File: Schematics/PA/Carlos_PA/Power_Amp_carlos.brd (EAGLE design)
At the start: 83.5 x 71.1 mm, 105 parts, among them J1 4_PIN_AMPCONN, U1 LME49830, U2 LME49830, U3 LME49830

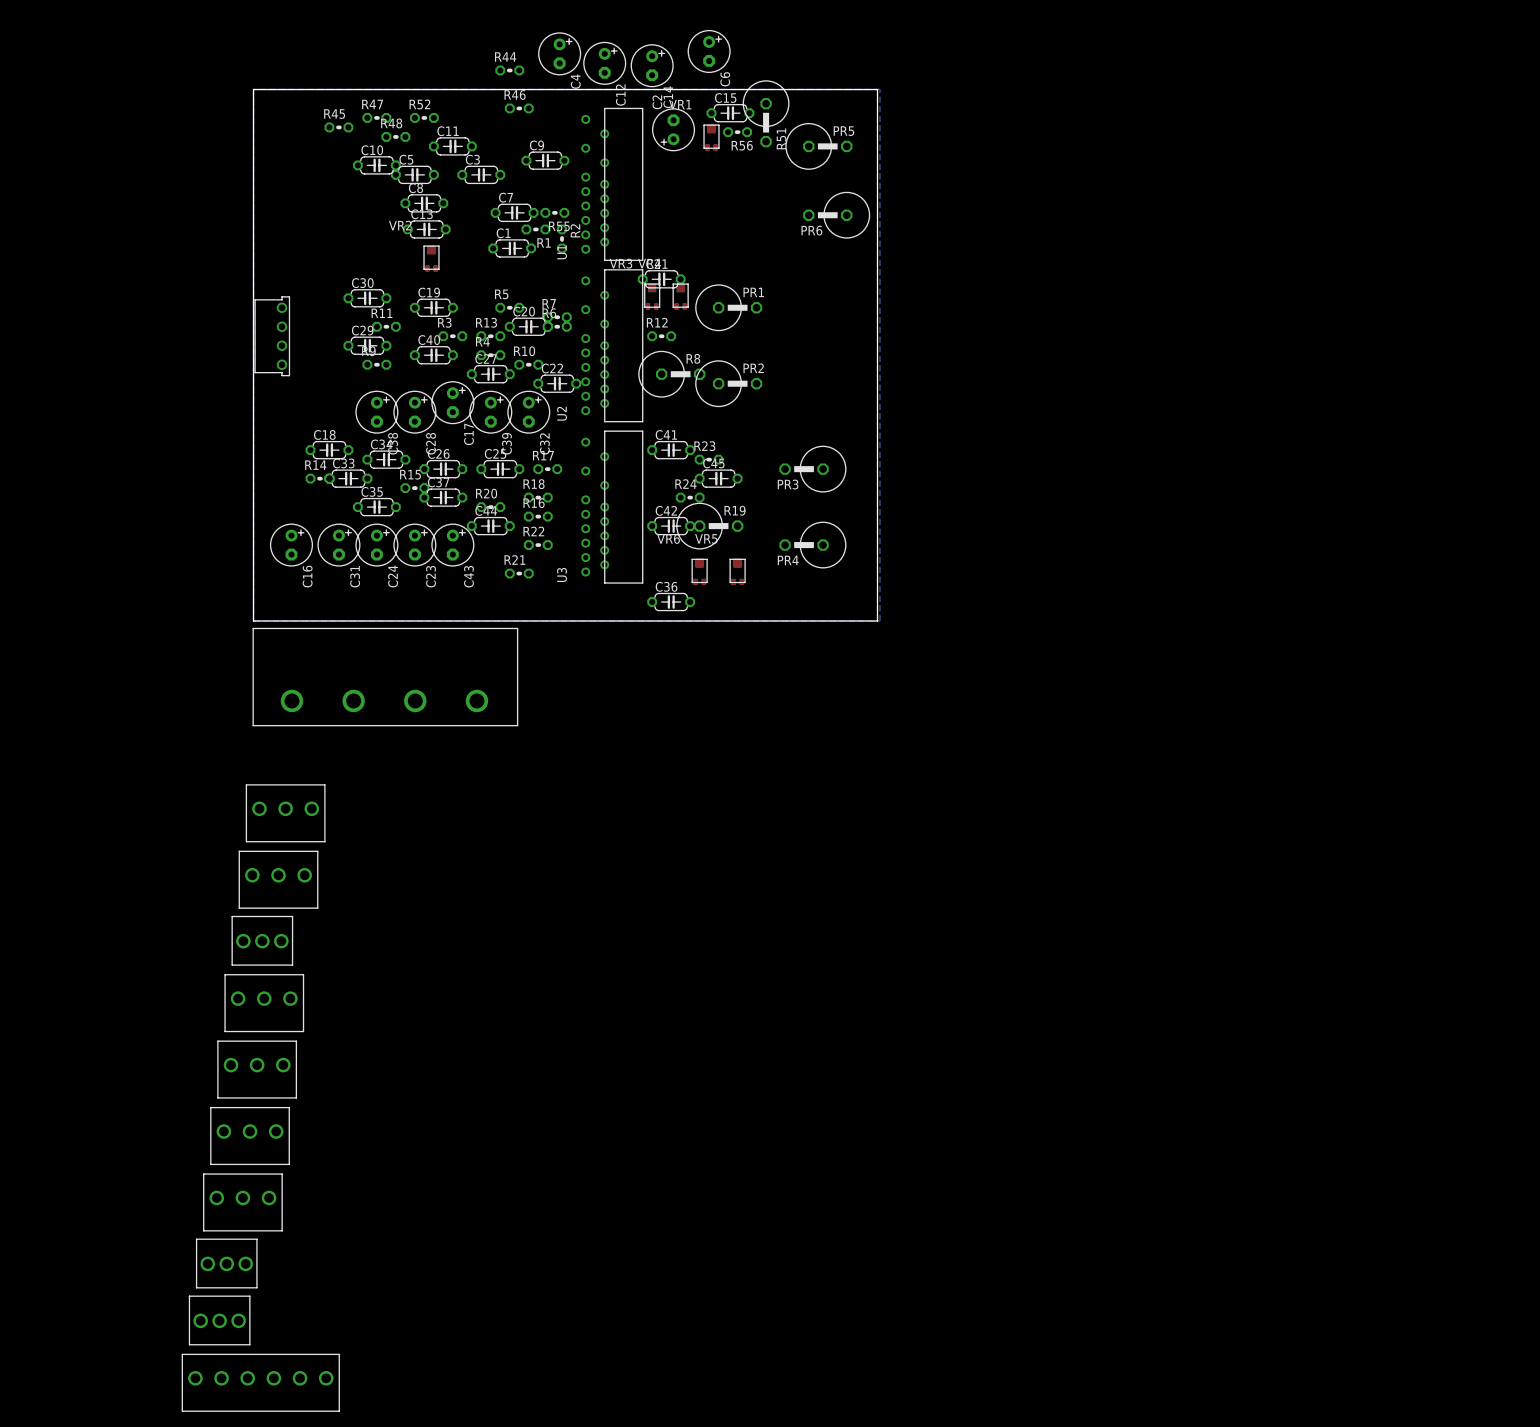
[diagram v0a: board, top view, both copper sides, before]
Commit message: fixed footprint of PA
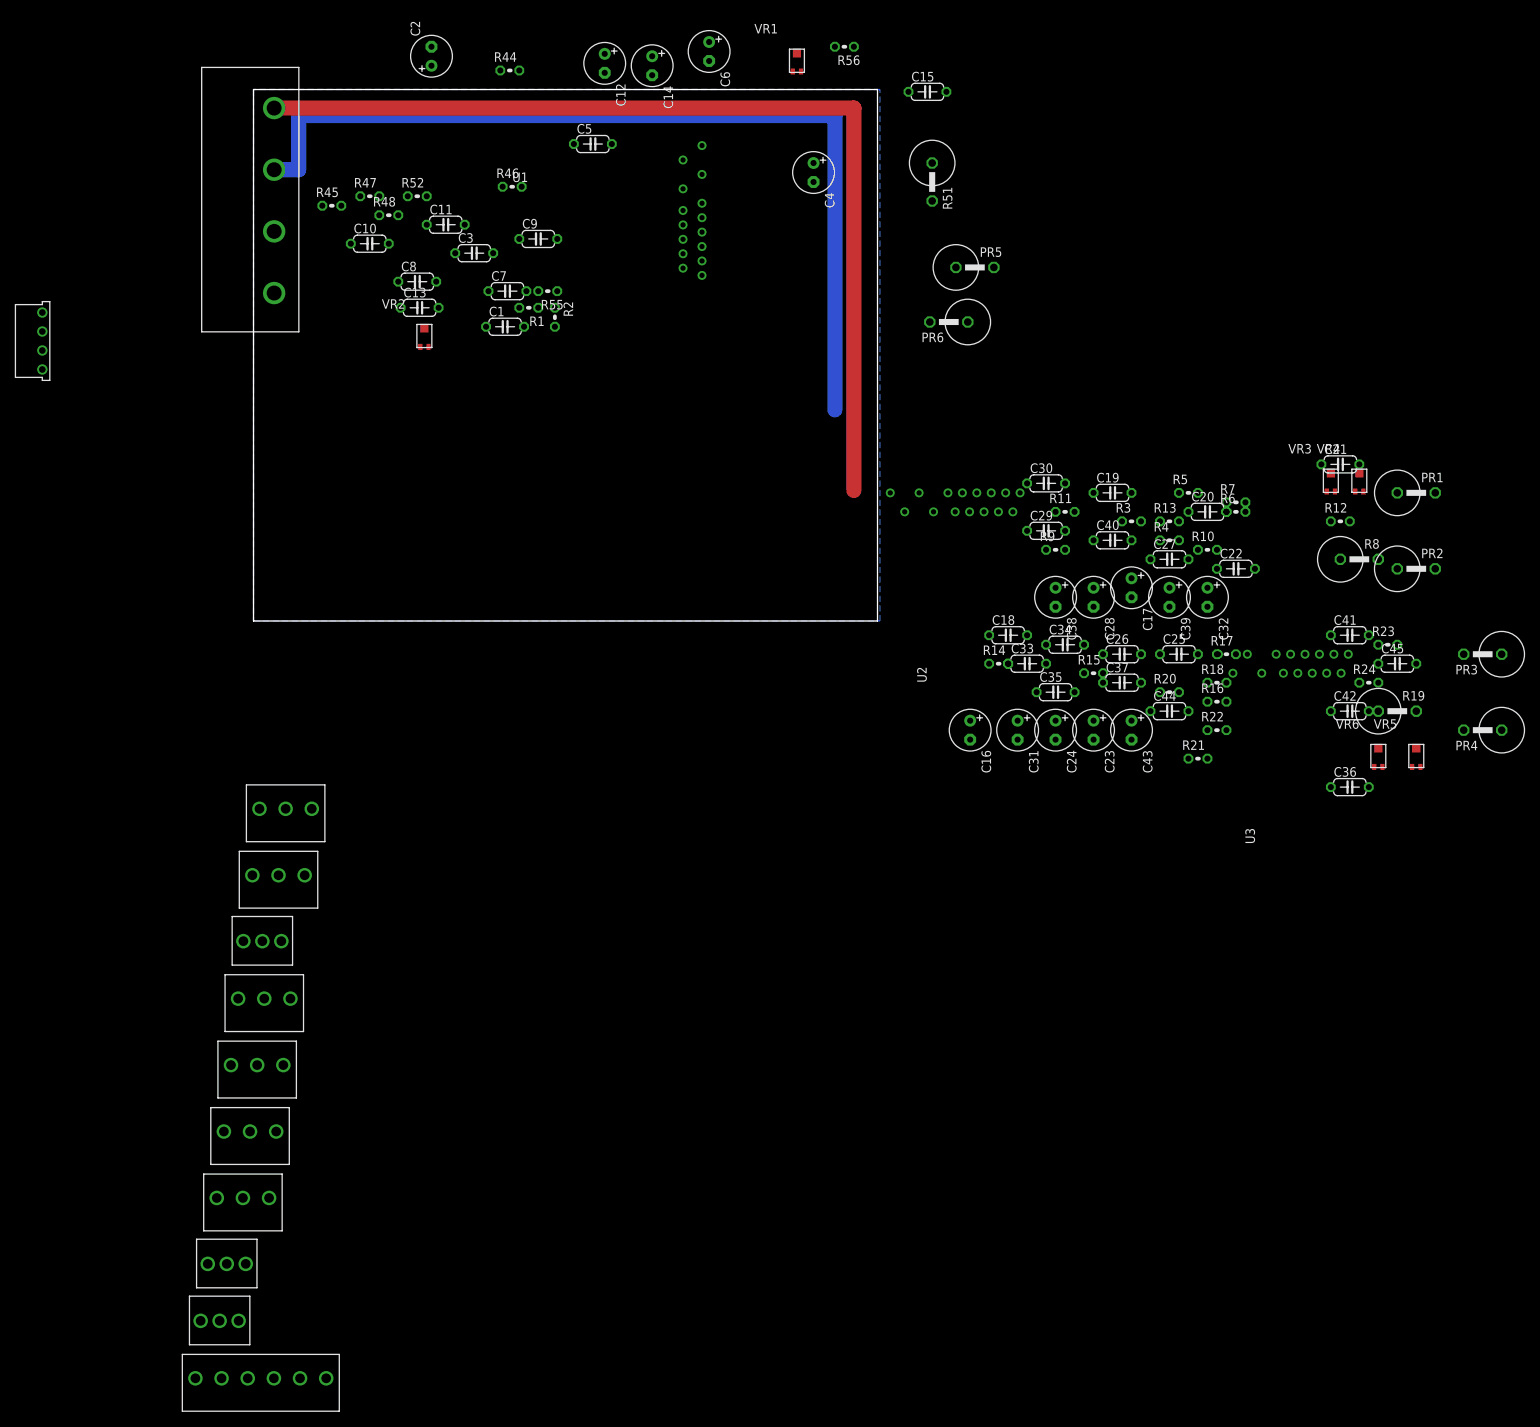
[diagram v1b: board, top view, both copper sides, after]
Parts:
- moved C16 94.1 mm to (95.9, -14.6)
- moved C18 94.1 mm to (101.0, -1.91)
- moved C19 94.1 mm to (114.9, 17.1)
- moved C20 94.1 mm to (127.6, 14.6)
- moved C25 94.1 mm to (123.8, -4.45)
- moved C26 94.1 mm to (116.2, -4.45)
- moved C27 94.1 mm to (122.6, 8.26)
- moved C29 94.1 mm to (106.0, 12.1)
- moved C30 94.1 mm to (106.0, 18.4)
- moved C31 94.1 mm to (102.2, -14.6)
- moved C32 94.1 mm to (127.6, 3.17)
- moved C36 94.1 mm to (146.7, -22.2)
- moved C37 94.1 mm to (116.2, -8.26)
- moved C39 94.1 mm to (122.6, 3.17)
- moved C40 94.1 mm to (114.9, 10.8)
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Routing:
- net V+: track 0.00 -> 128.7 mm
- net V-: track 0.00 -> 121.6 mm

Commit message: did dome work on my PA board
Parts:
- moved C47 119.6 mm to (70.2, 66.7), turned to 270 degrees
- moved C48 113.3 mm to (55.9, 59.1), turned to 270 degrees
- moved U3 97.9 mm to (42.2, 11.7), turned to 0 degrees
- moved U2 56.2 mm to (41.9, 33.4), turned to 0 degrees
- moved R48 48.4 mm to (66.0, 61.0), turned to 90 degrees
- moved R47 43.9 mm to (59.1, 62.5), turned to 90 degrees
- moved C11 41.3 mm to (65.1, 65.4), turned to 180 degrees
- moved C15 35.0 mm to (65.4, 46.0)
- moved C13 34.6 mm to (54.6, 54.0)
- moved C4 31.5 mm to (43.8, 65.1), turned to 0 degrees
- moved C9 30.4 mm to (12.4, 34.9)
- moved PR5 30.0 mm to (67.0, 52.4)
- moved R46 27.7 mm to (62.2, 59.7)
- moved C12 26.3 mm to (70.5, 62.9)
- moved PR6 26.2 mm to (71.4, 54.9), turned to 315 degrees
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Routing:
- net N$4: track 0.00 -> 33.1 mm
- net V+: track 128.7 -> 159.7 mm
- net V-: track 121.6 -> 148.5 mm, vias 0 -> 1
- net N$70: track 0.00 -> 22.4 mm
- net N$72: track 0.00 -> 13.0 mm
- net N$73: track 0.00 -> 11.5 mm
- net N$110: track 0.00 -> 9.09 mm
- net N$75: track 0.00 -> 8.19 mm
- net N$74: track 0.00 -> 5.35 mm

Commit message: more work on my Pa brd
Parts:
- moved C46 106.7 mm to (42.5, 50.5)
- moved J1 49.8 mm to (21.3, 32.4)
- moved C10 45.3 mm to (52.1, 59.7), turned to 180 degrees
- moved C6 44.9 mm to (27.9, 45.7), turned to 90 degrees
- moved R56 42.8 mm to (45.1, 50.8)
- moved R45 41.4 mm to (51.4, 56.5)
- moved VR1 39.5 mm to (41.0, 51.1)
- moved C9 37.8 mm to (41.3, 59.4), turned to 180 degrees
- moved VR2 31.8 mm to (47.3, 58.1)
- moved C8 23.4 mm to (42.5, 56.5)
- moved R44 21.9 mm to (53.0, 62.2)
- moved C7 21.6 mm to (47.9, 47.9), turned to 180 degrees
- moved R2 17.5 mm to (29.5, 50.8)
- moved U2 16.5 mm to (57.5, 28.0)
- moved U$5 16.2 mm to (19.7, 57.1)
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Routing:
- net N$75: track 8.19 -> 81.7 mm
- net N$85: track 0.00 -> 25.3 mm
- net N$69: track 0.00 -> 21.9 mm
- net MUTE: track 0.00 -> 18.4 mm
- net V+: track 159.7 -> 141.4 mm
- net N$67: track 0.00 -> 18.3 mm
- net N$65: track 0.00 -> 12.7 mm, vias 0 -> 1
- net N$66: track 0.00 -> 11.6 mm
- net N$68: track 0.00 -> 10.1 mm
- net N$16: track 0.00 -> 8.94 mm
- net N$31: track 0.00 -> 7.09 mm
- net N$40: track 0.00 -> 5.82 mm
- net N$36: track 0.00 -> 3.49 mm
- net V-: track 148.5 -> 151.9 mm, vias 1 -> 0

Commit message: finished my PA board
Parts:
- moved C55 179.6 mm to (81.3, 49.2), turned to 270 degrees
- moved C50 127.7 mm to (67.3, 41.6), turned to 270 degrees
- moved C53 122.5 mm to (41.9, 22.9)
- moved R12 108.0 mm to (37.8, 22.5)
- moved C49 106.4 mm to (52.7, 35.2), turned to 270 degrees
- moved VR3 105.4 mm to (39.4, 29.5)
- moved R10 103.8 mm to (25.1, 25.7)
- moved VR4 103.0 mm to (46.0, 33.3)
- moved C21 95.2 mm to (51.1, 34.3), turned to 180 degrees
- moved C22 94.1 mm to (41.3, 34.0)
- moved C19 93.2 mm to (26.4, 46.0), turned to 180 degrees
- moved PR1 93.0 mm to (63.2, 27.6)
- moved C28 91.6 mm to (25.7, 32.7), turned to 180 degrees
- moved PR2 91.1 mm to (67.6, 30.8), turned to 315 degrees
- moved C20 89.3 mm to (41.3, 37.1), turned to 180 degrees
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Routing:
- net N$12: track 0.00 -> 84.7 mm, vias 0 -> 1
- net V-: track 151.9 -> 234.9 mm
- net V+: track 141.4 -> 211.5 mm, vias 0 -> 2
- net N$15: track 0.00 -> 30.5 mm
- net RIGHT: track 0.00 -> 29.8 mm
- net N$75: track 81.7 -> 109.0 mm
- net N$5: track 0.00 -> 25.8 mm
- net N$7: track 0.00 -> 21.4 mm
- net N$3: track 0.00 -> 21.1 mm
- net N$2: track 0.00 -> 21.0 mm
- net N$14: track 0.00 -> 15.9 mm
- net N$68: track 10.1 -> 25.3 mm
- net N$1: track 0.00 -> 14.3 mm, vias 0 -> 2
- net N$9: track 0.00 -> 13.8 mm
- net N$8: track 0.00 -> 12.4 mm
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- added copper zone on layer 1, net GND
